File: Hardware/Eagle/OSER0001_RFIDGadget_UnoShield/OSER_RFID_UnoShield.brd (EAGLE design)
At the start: 68.8 x 53.5 mm, 6 parts, among them U1 ARDUINOR3-BPLACE

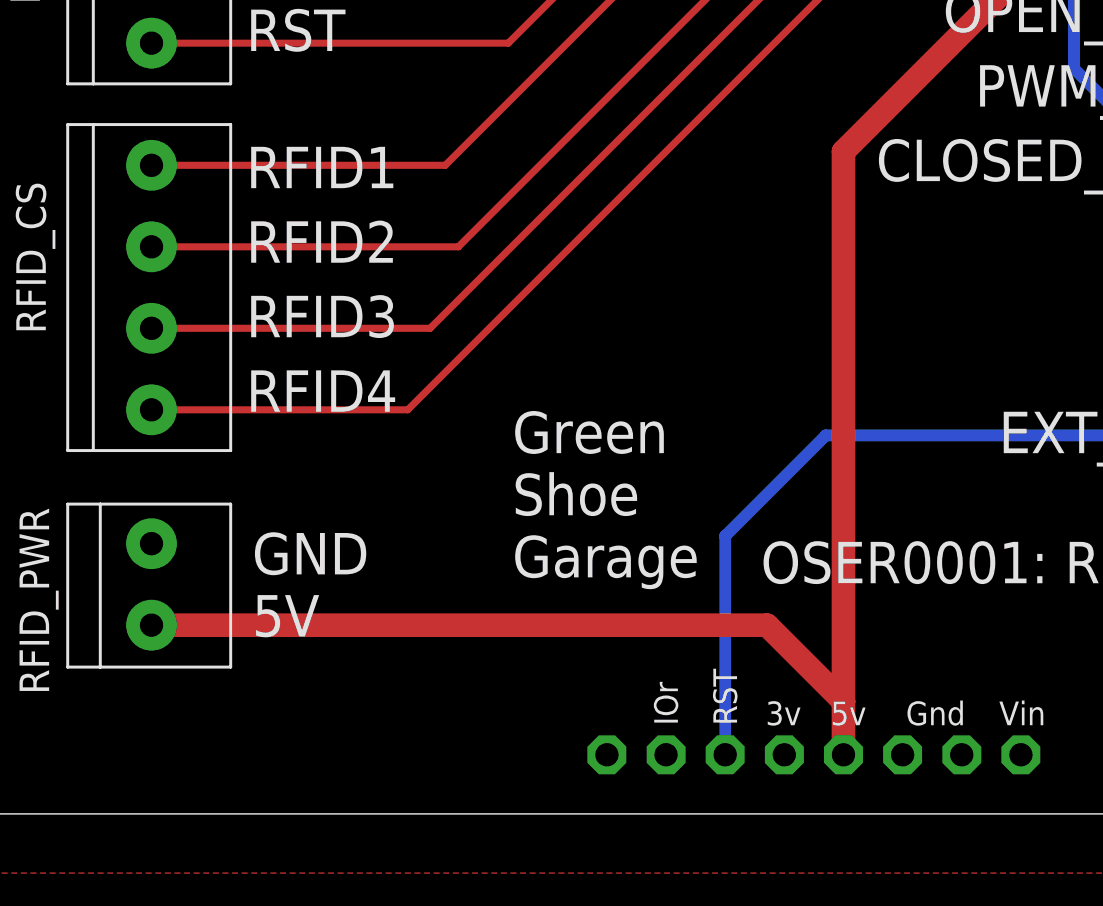
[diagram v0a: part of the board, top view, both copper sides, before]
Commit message: 1x3 header pin to allow user select 3V or 5V to RFID reader
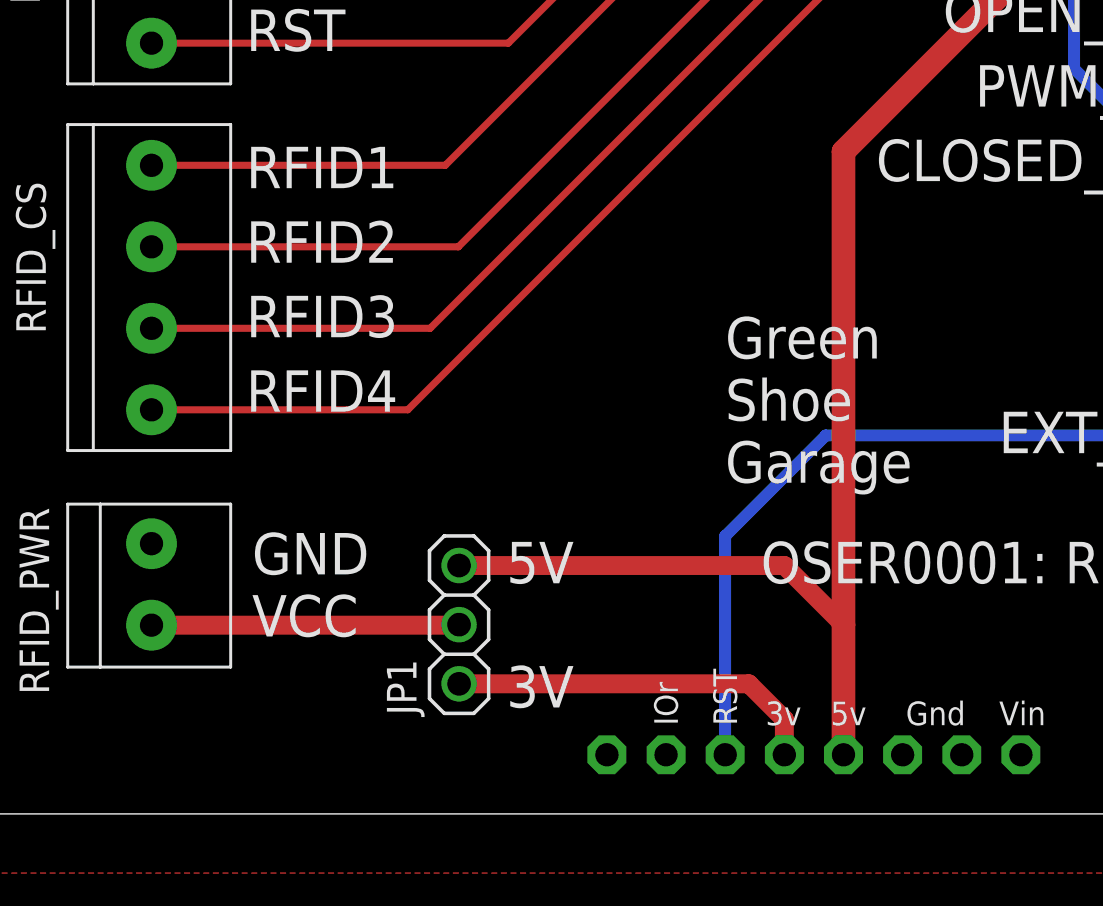
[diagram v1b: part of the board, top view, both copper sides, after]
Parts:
- added JP1: (no value), adafruit:1X03
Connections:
- new net N$1: JP1.2, RFID_PWR.1
- net PWR_3V: now also JP1.1
- net PWR_5V: now also JP1.3; no longer RFID_PWR.1
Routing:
- net PWR_3V: track 0.00 -> 16.1 mm
- net PWR_5V: track 81.3 -> 67.8 mm
- net N$1: track 0.00 -> 13.2 mm
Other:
- board text added: "5V 3V"
- board text added: "GND VCC"
- board text removed: "GND 5V"
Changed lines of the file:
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@@
 </layers>
 <board>
-<fusionsync huburn="a.cGVyc29uYWw6dWUyOWJjZWYx" projecturn="a.cGVyc29uYWw6dWUyOWJjZWYxI0QyMDE1MDcxMjE0NTU5MDgx" f3durn="urn:adsk.wipprod:dm.lineage:w13Q8Y1uQFOl_O_fl7fG8A" pcbguid="af29fb43-534a-4a97-9497-6bcbfa06ad60" lastpulledtime="" lastsyncedchangeguid="6569aadf-e001-3e28-3366-a9aad11297b7"/>
+<fusionsync huburn="a.cGVyc29uYWw6dWUyOWJjZWYx" projecturn="a.cGVyc29uYWw6dWUyOWJjZWYxI0QyMDE1MDcxMjE0NTU5MDgx" f3durn="urn:adsk.wipprod:dm.lineage:w13Q8Y1uQFOl_O_fl7fG8A" pcbguid="af29fb43-534a-4a97-9497-6bcbfa06ad60" lastpulledtime="" lastsyncedchangeguid="b97f2190-8900-7f2f-96dc-16017b6e0a3a"/>
 <plain>
 <wire x1="0" y1="0" x2="68.814" y2="0" width="0" layer="20"/>
@@
 MOSI
 RST</text>
-<text x="23.876" y="10.16" size="1.778" layer="21">Green
+<text x="33.02" y="14.224" size="1.778" layer="21">Green
 Shoe
 Garage</text>
@@
 RFID4</text>
 <text x="12.7" y="7.62" size="1.778" layer="21">GND
-5V</text>
+VCC</text>
 <text x="54.356" y="15.494" size="1.778" layer="21" align="bottom-right">GND
 EXT_RST</text>
@@
 PWM_PIN
 CLOSED_LED</text>
+<text x="23.622" y="4.572" size="1.778" layer="21">5V
+3V</text>
 </plain>
 <attributes>
@@
 <attribute name="NAME" x="63.634" y="28.464" size="1.27" layer="25" rot="R90"/>
 </element>
+<element name="JP1" library="adafruit" library_urn="urn:adsk.eagle:library:420" package="1X03" package3d_urn="urn:adsk.eagle:package:6240710/1" override_package3d_urn="urn:adsk.eagle:package:12983531/2" override_package_urn="urn:adsk.eagle:footprint:6240064/1" value="" x="21.59" y="8.128" smashed="yes" rot="R90">
+<attribute name="NAME" x="19.7612" y="4.2418" size="1.27" layer="25" ratio="10" rot="R90"/>
+<attribute name="VALUE" x="24.765" y="4.318" size="1.27" layer="27" rot="R90"/>
+</element>
 </elements>
 <signals>
@@
 <signal name="PWR_3V">
 <contactref element="U1" pad="3V"/>
+<contactref element="JP1" pad="1"/>
+<wire x1="21.59" y1="5.588" x2="34.036" y2="5.588" width="0.8128" layer="1"/>
+<wire x1="34.036" y1="5.588" x2="35.56" y2="4.064" width="0.8128" layer="1"/>
+<wire x1="35.56" y1="4.064" x2="35.56" y2="2.54" width="0.8128" layer="1"/>
 </signal>
 <signal name="EXT_MASTER_RST">
@@
 <contactref element="U1" pad="5V"/>
 <contactref element="ACTUATORS" pad="4"/>
-<wire x1="38.1" y1="2.54" x2="38.1" y2="4.826" width="1.016" layer="1"/>
-<wire x1="38.1" y1="4.826" x2="38.1" y2="28.448" width="1.016" layer="1"/>
+<wire x1="38.1" y1="2.54" x2="38.1" y2="8.128" width="1.016" layer="1"/>
+<wire x1="38.1" y1="8.128" x2="38.1" y2="28.448" width="1.016" layer="1"/>
 <wire x1="38.1" y1="28.448" x2="47.752" y2="38.1" width="1.016" layer="1"/>
 <wire x1="47.752" y1="38.1" x2="58.364" y2="38.1" width="1.016" layer="1"/>
 <wire x1="58.364" y1="38.1" x2="58.42" y2="38.044" width="1.016" layer="1"/>
-<contactref element="RFID_PWR" pad="1"/>
-<wire x1="8.382" y1="8.106" x2="34.82" y2="8.106" width="1.016" layer="1"/>
-<wire x1="34.82" y1="8.106" x2="38.1" y2="4.826" width="1.016" layer="1"/>
+<contactref element="JP1" pad="3"/>
+<wire x1="21.59" y1="10.668" x2="35.56" y2="10.668" width="0.8128" layer="1"/>
+<wire x1="35.56" y1="10.668" x2="38.1" y2="8.128" width="0.8128" layer="1"/>
 </signal>
 <signal name="CLOSED_LED">
@@
 <wire x1="58.42" y1="46.482" x2="58.42" y2="50.8" width="0.508" layer="16"/>
 </signal>
+<signal name="N$1">
+<contactref element="RFID_PWR" pad="1"/>
+<contactref element="JP1" pad="2"/>
+<wire x1="8.382" y1="8.106" x2="21.568" y2="8.106" width="0.8128" layer="1"/>
+<wire x1="21.568" y1="8.106" x2="21.59" y2="8.128" width="0.8128" layer="1"/>
+</signal>
 </signals>
